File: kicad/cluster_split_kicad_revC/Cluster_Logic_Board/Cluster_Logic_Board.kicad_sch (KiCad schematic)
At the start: 28 parts, among them J1 5V LOGIC POWER IN, J10 TO CLUSTER SERVO BOARD — UNCH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, J2 0.96in SSD1306 OLED, J3 PIR LEFT, J4 PIR CENTER, J5 PIR RIGHT, SW1 CLUSTER ID DIP, U1 Hosyond ESP32-S3 N16R8 Dev Bo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, U2 WWZMDiB DFPlayer Mini #1, U3 WWZMDiB DFPlayer Mini #2

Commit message: Anotther initial starting version of Controller Logic PCB
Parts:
- added C7: 47uF 10V, Capacitor_THT:CP_Radial_D5.0mm_P2.00mm, symbol Cluster:C2
- added C8: 100nF, Capacitor_THT:C_Disc_D5.0mm_W2.5mm_P5.00mm, symbol Cluster:C2
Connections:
- net +5V_LOGIC: now also C7.1 (+), C8.1 (+)
- net GND: now also C7.2 (-), C8.2 (-)
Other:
- note added: "ESP32 LOCAL 5V DECOUPLING — PLACE PHYSICALLY CLOSE TO U1 VIN/GND"
- title: Cluster Logic Board Rev C -> Cluster Logic Board Rev E

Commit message: YET Anotther initial starting version of Controller Logic PCB
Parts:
- removed U1: Hosyond ESP32-S3 N16R8 Dev Board, Halloween:Hosyond_ESP32-S3_N16R8_44P, symbol MCU_Espressif:ESP32-S3
- added U1: Hosyond ESP32-S3 N16R8 44-pin DevKit, Halloween:Hosyond_ESP32-S3_N16R8_44P, symbol Cluster:DEVKIT44
- C2: value 47uF 10V -> 47uF 10V DF1
- C3: value 100nF -> 100nF DF1
- C4: value 47uF 10V -> 47uF 10V DF2
- C5: value 100nF -> 100nF DF2
- C7: value 47uF 10V -> 47uF 10V ESP32
- C8: value 100nF -> 100nF ESP32
- J10: value TO CLUSTER SERVO BOARD — UNCHANGED -> TO CLUSTER SERVO BOARD — DO NOT CHANGE
- SW1: value CLUSTER ID DIP -> CLUSTER ID
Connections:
- net +3V3_LOGIC: now also U1.J1.21 (5V), U1.J1.22 (GND)
- net +5V_LOGIC: now also U1.J1.2 (3V3)
- net DF1_TX: now also U1.J1.12 (GPIO8)
- net DF2_TX: now also U1.J1.14 (GPIO46)
- net GND: now also U1.J1.1 (3V3), U1.J3.1 (GND), U1.J3.2 (GPIO43/TX0), U1.J3.22 (GND)
- net I2C_SCL: now also U1.J1.8 (GPIO15)
- net I2C_SDA: now also U1.J1.11 (GPIO18)
- net ID0: now also U1.J1.19 (GPIO13)
- net ID1: now also U1.J1.18 (GPIO12)
- net ID2: now also U1.J1.17 (GPIO11)
- net ID3: now also U1.J1.16 (GPIO10)
- net LED_DATA_3V3: now also U1.J1.7 (GPIO7)
- net PCA_OE_N: now also U1.J1.3 (EN/RST)
- net PIR_CENTER: now also U1.J1.5 (GPIO5)
- net PIR_LEFT: now also U1.J1.6 (GPIO6)
- net PIR_RIGHT: now also U1.J1.4 (GPIO4)
- net DF1_ESP_TX renamed DF1_RX_ESP
- net DF1_RX_ESP: now also U1.J1.13 (GPIO3)
- net DF2_ESP_TX renamed DF2_RX_ESP
- net DF2_RX_ESP: now also U1.J1.15 (GPIO9)
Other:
- note added: "Arduino GPIO assignments: ID0..3=4,5,6,7; SDA=8; SCL=9; LED_DATA=10; PIR L/C/R=11,12,13; PCA_OE=14; DF2 TX/RX=15/16; DF1 TX/RX=17/18."
- note added: "CLUSTER LOGIC BOARD REV G — U1 REBUILT FROM PHYSICAL DEVKIT HEADERS"
- note added: "J10 UNCHANGED: 1 GND | 2 GND | 3 3V3 | 4 SDA | 5 SCL | 6 LED_DATA | 7 PCA_OE_N | 8 SPARE"
- note added: "U1 pin numbers are literal DevKit header locations (J1.x / J3.x). 5V = U1:J1.21. GND = U1:J1.22, J3.1, J3.21, J3.22. 3V3 = U1:J1.1/J1.2."
- note added: "Unused by design: GPIO0/3/45/46 strapping-related; GPIO19/20 native USB; GPIO35/36/37 reserved on octal PSRAM variants; GPIO43/44 left free for UART0/programming."
- note removed: "CLUSTER LOGIC BOARD REV C — FIXED MODERN KICAD SCHEMATIC"
- note removed: "DFPlayer Mini footprint: standard 16-pin DFR0299/MP3-TF-16P style. J10 remains exactly: GND,GND,3V3,SDA,SCL,LED_DATA,PCA_OE,SPARE."
- note removed: "DFPlayer standard pinout used: 1 VCC, 2 RX, 3 TX, 4 DAC_R, 5 DAC_L, 6 SPK1, 7 GND, 8 SPK2, 9 IO1, 10 GND, 11 IO2, 12 ADKEY1, 13 ADKEY2, 14 USB+, 15 USB-, 16 BUSY."
- note removed: "ESP32 LOCAL 5V DECOUPLING — PLACE PHYSICALLY CLOSE TO U1 VIN/GND"
- title: Cluster Logic Board Rev E -> Cluster Logic Board Rev G

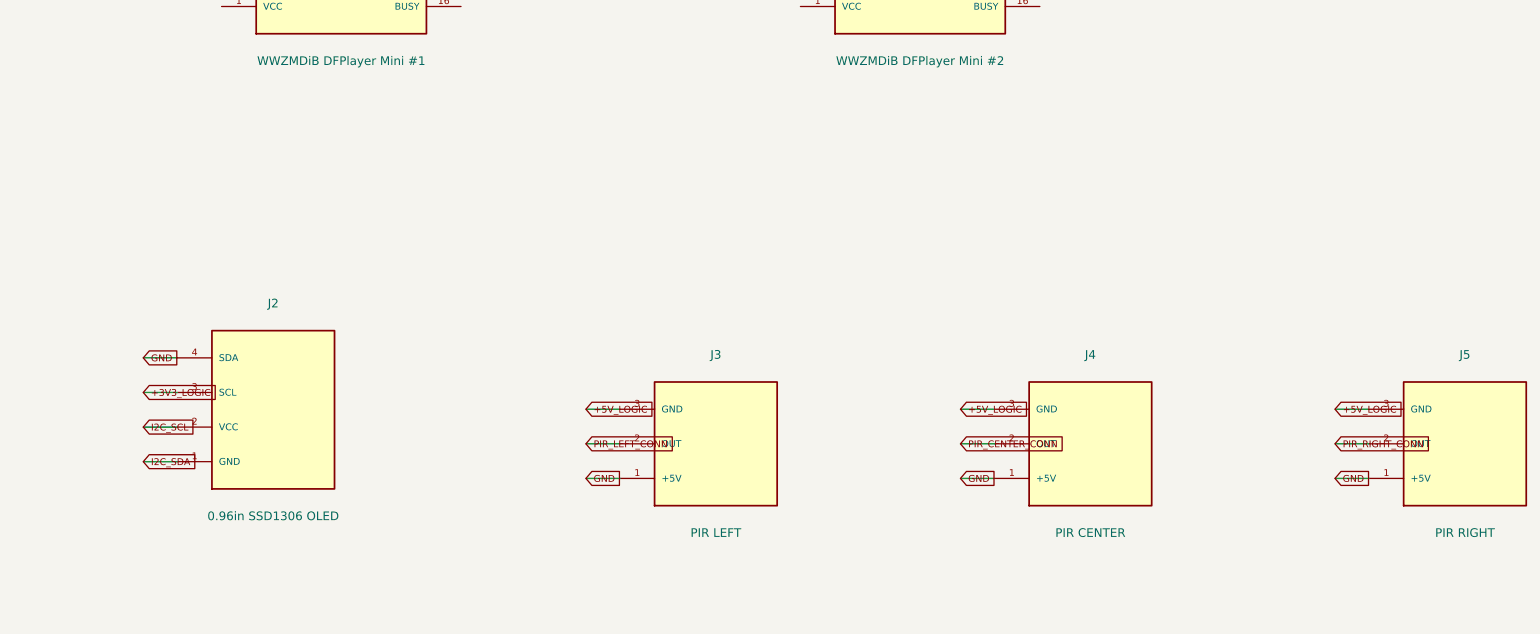
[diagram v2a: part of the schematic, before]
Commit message: Fixed servo controller footprint, submitted to JLCPCB today
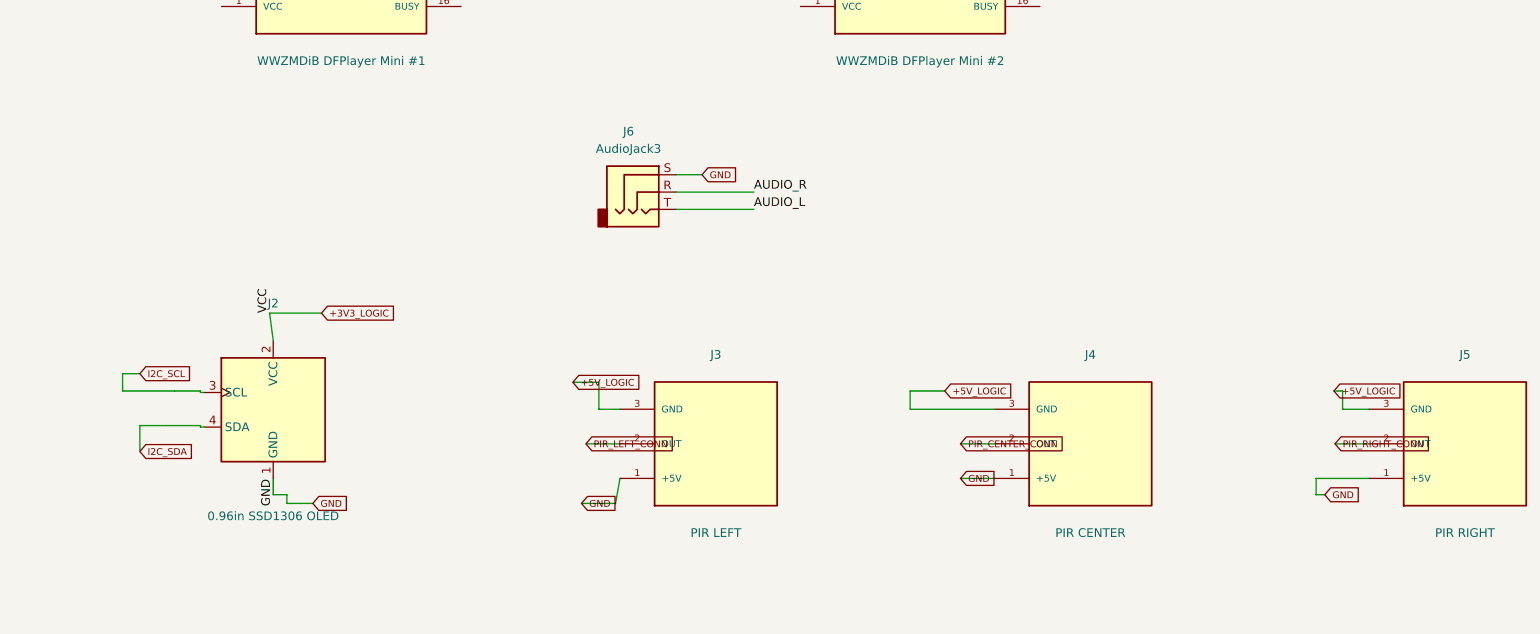
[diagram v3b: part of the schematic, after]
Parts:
- added J6: AudioJack3, symbol Connector_Audio:AudioJack3
- J2: footprint Halloween:OLED_SSD1306_096_4P -> Display:ER_OLEDM0.91_1x-I2C; symbol Cluster:OLED4 -> Display_Graphic:ER_OLEDM0.91_1x-I2C
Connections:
- net +3V3_LOGIC: now also J2.2 (VCC); no longer J2.3 (SCL)
- net GND: now also J2.1 (GND), J6.S; no longer J2.4 (SDA)
- net I2C_SCL: now also J2.3 (SCL); no longer J2.2 (VCC)
- net I2C_SDA: now also J2.4 (SDA); no longer J2.1 (GND)
- new net AUDIO_L: J6.T
- new net AUDIO_R: J6.R
